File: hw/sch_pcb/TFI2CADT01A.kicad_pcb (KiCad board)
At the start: 2 copper layers, 25 x 23 mm, 38 parts, among them J1 SM04B-GHS-TB, J2 SM04B-GHS-TB, J3 SM04B-GHS-TB, J4 SM04B-GHS-TB, J5 SM04B-GHS-TB, J6 SM04B-GHS-TB, M1 HOLE, M2 HOLE, M3 HOLE, M4 HOLE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

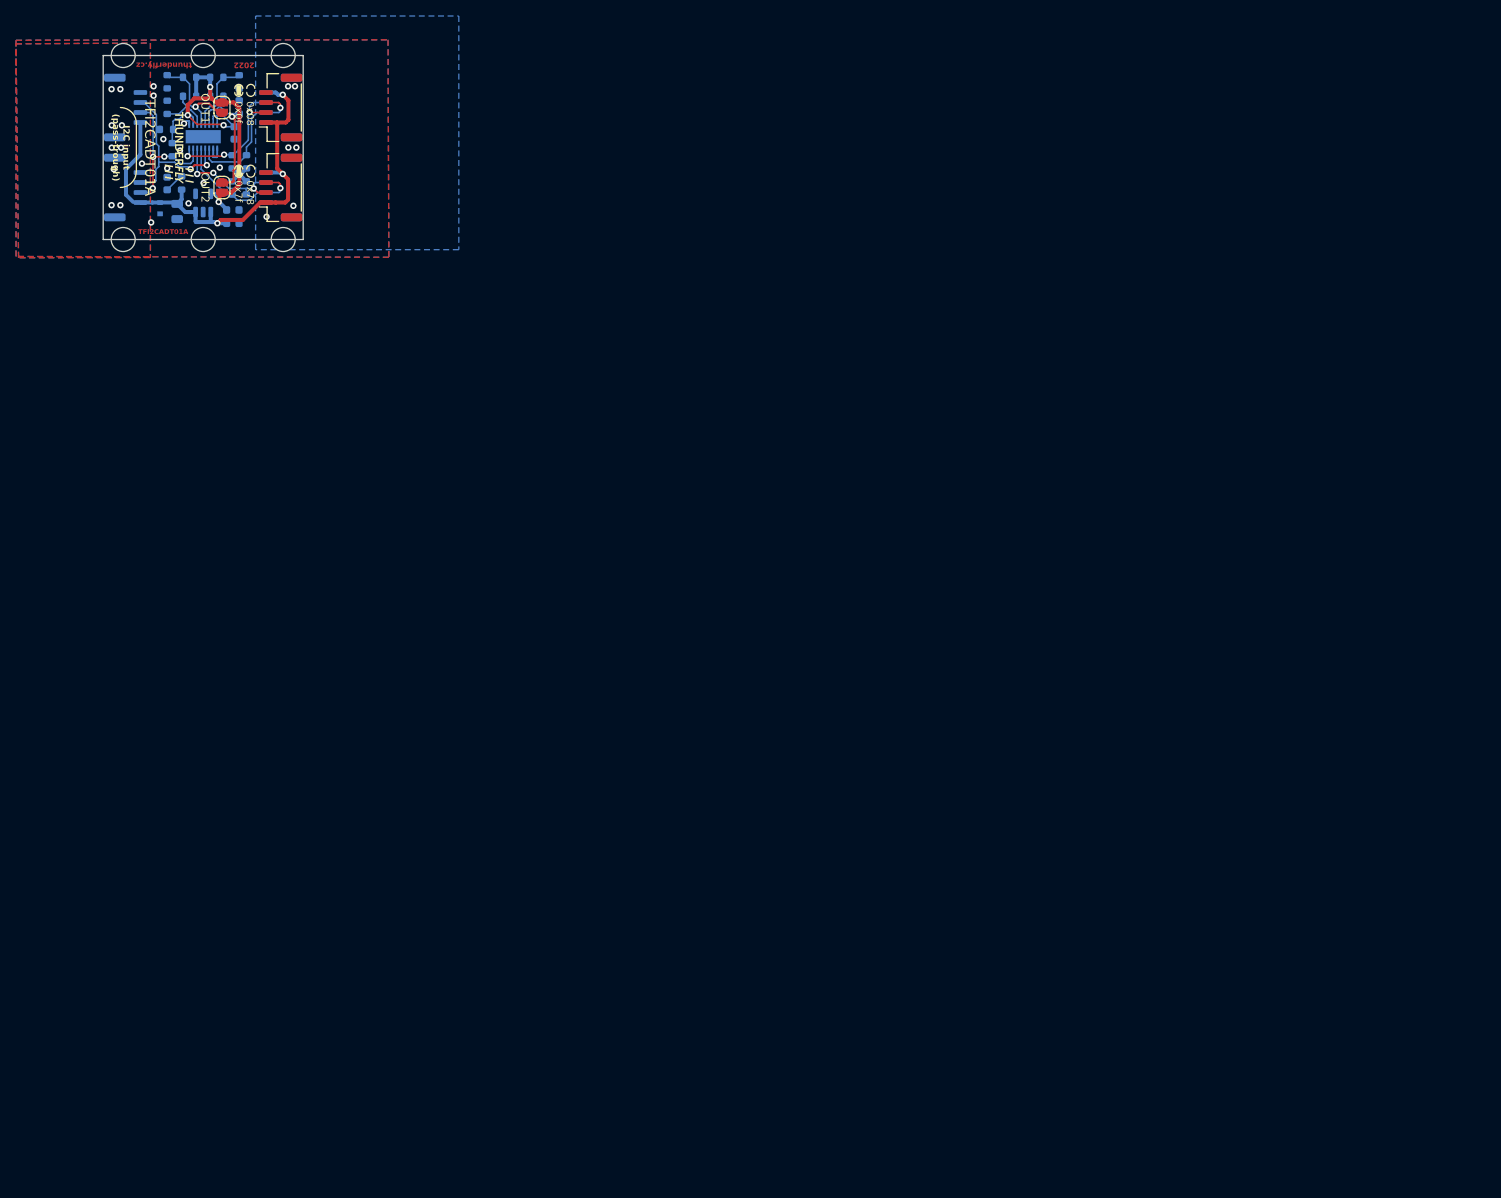
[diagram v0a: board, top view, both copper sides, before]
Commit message: Update Titleblock Move PCB to center of the page Move grid origin to the bottom left corner of the PCB
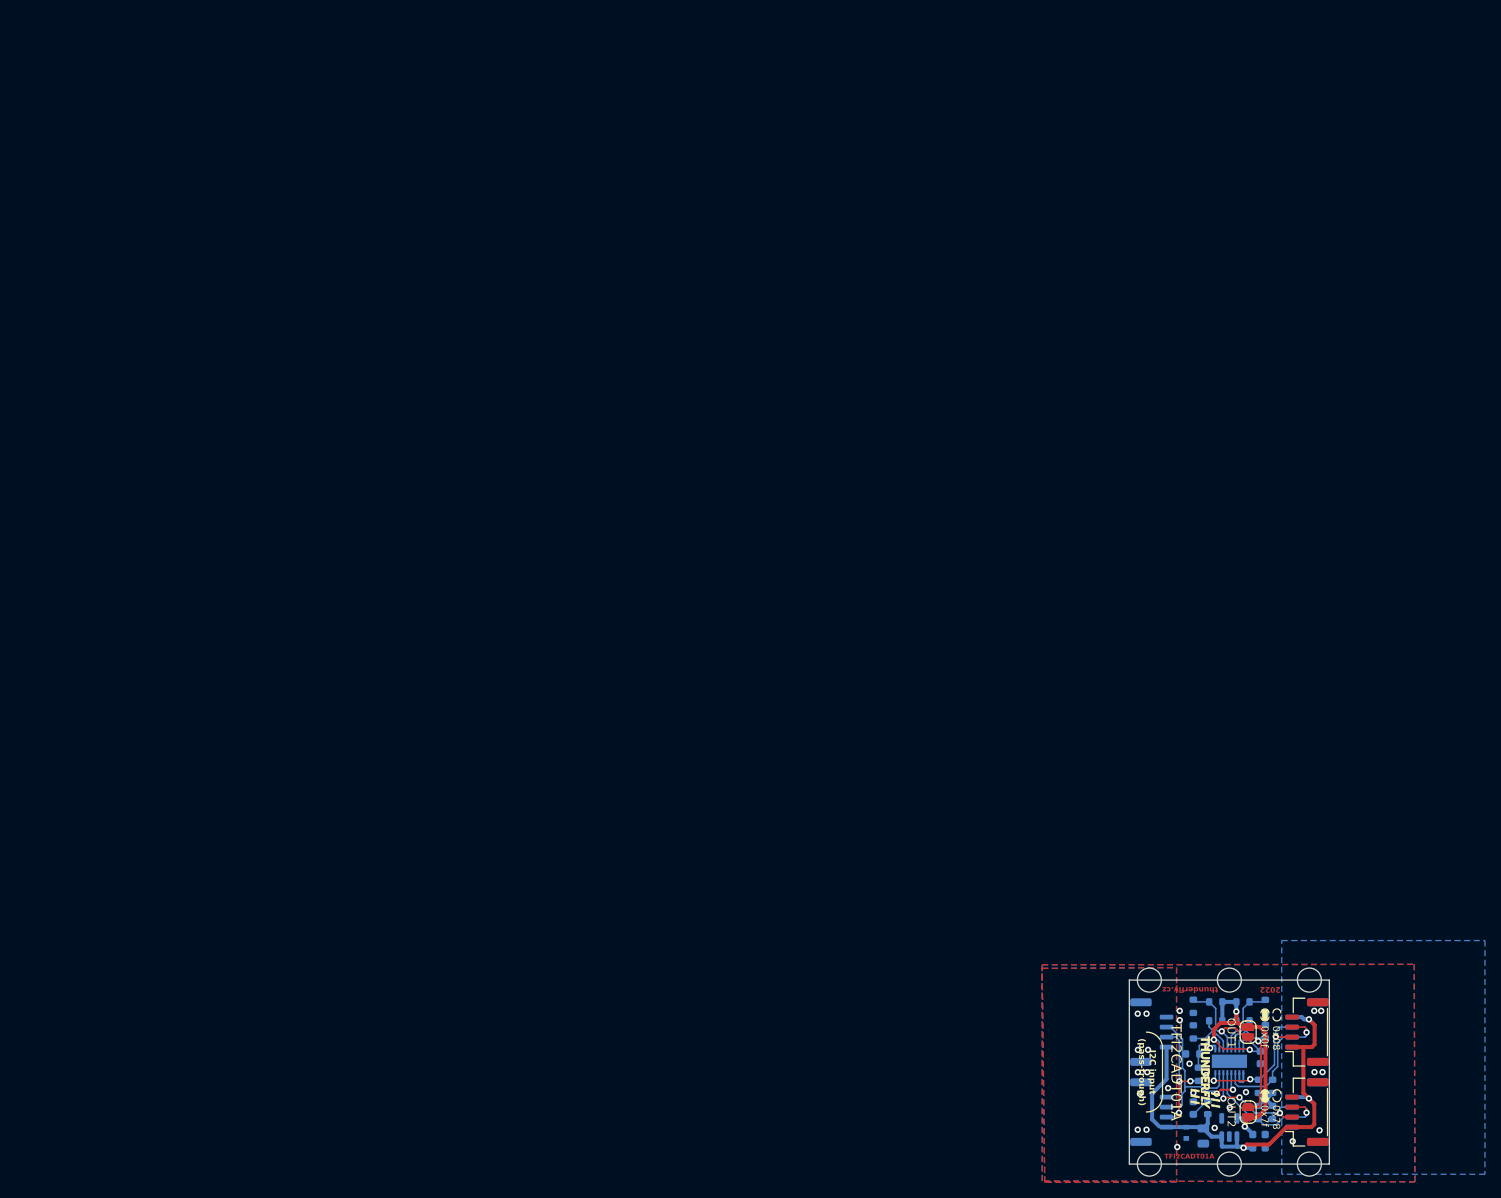
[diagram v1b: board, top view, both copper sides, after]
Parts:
- moved C1 172.7 mm to (137.5, 112.1)
- moved C2 172.7 mm to (144.5, 113.5)
- moved C3 172.7 mm to (144.5, 111.9)
- moved D1 172.7 mm to (136.3, 108.6)
- moved D2 172.7 mm to (135.4, 111.7)
- moved G1 172.7 mm to (137.8, 104.1)
- moved J3 172.7 mm to (150.5, 109.1)
- moved J4 172.7 mm to (150.5, 109.1)
- moved J5 172.7 mm to (150.5, 99.1)
- moved J6 172.7 mm to (150.5, 99.1)
- moved JP1 172.7 mm to (143.1, 109.1)
- moved JP2 172.7 mm to (143.1, 99.1)
- moved M1 172.7 mm to (140.8, 115.6)
- moved M2 172.7 mm to (140.8, 92.6)
- moved M3 172.7 mm to (130.8, 115.6)
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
